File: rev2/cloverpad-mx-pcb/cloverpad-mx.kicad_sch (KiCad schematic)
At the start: 42 parts, among them J1 USB_C_Receptacle_USB2.0, SW1 SW_Push, SW2 SW_Push, U1 SRV05-4, U2 XC6206P332MR, U8 RP2040, U9 W25Q16JVSSIQ, Y1 12MHz

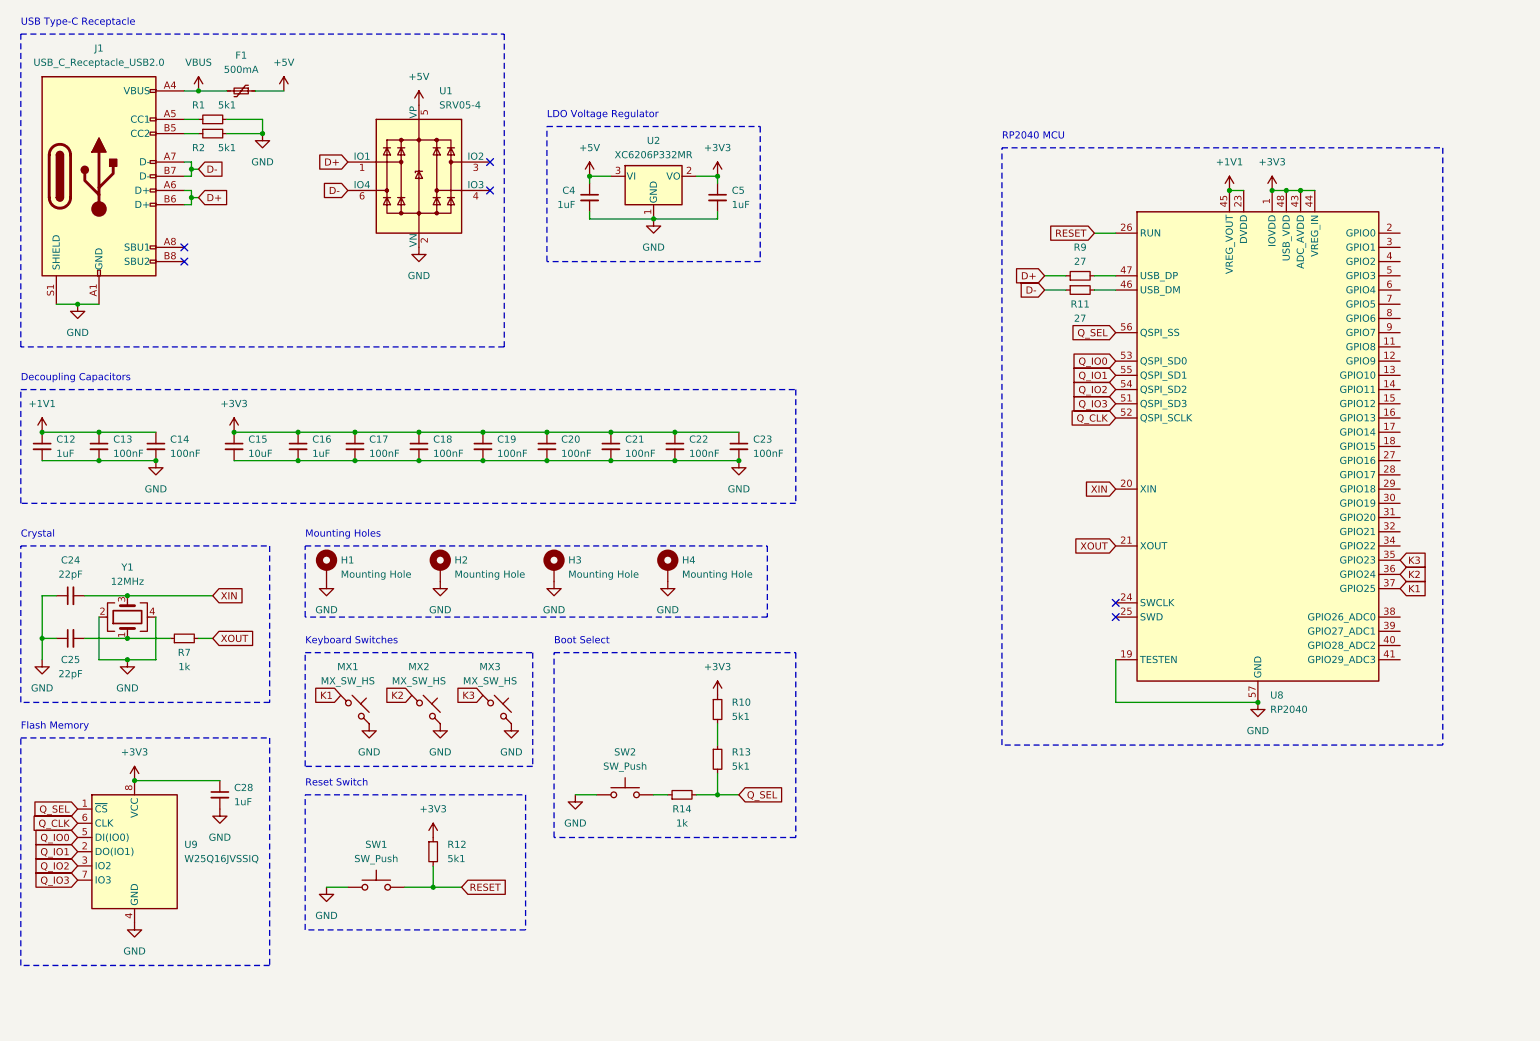
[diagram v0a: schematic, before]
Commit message: chore: update all symbols + footprints to match kicad 8
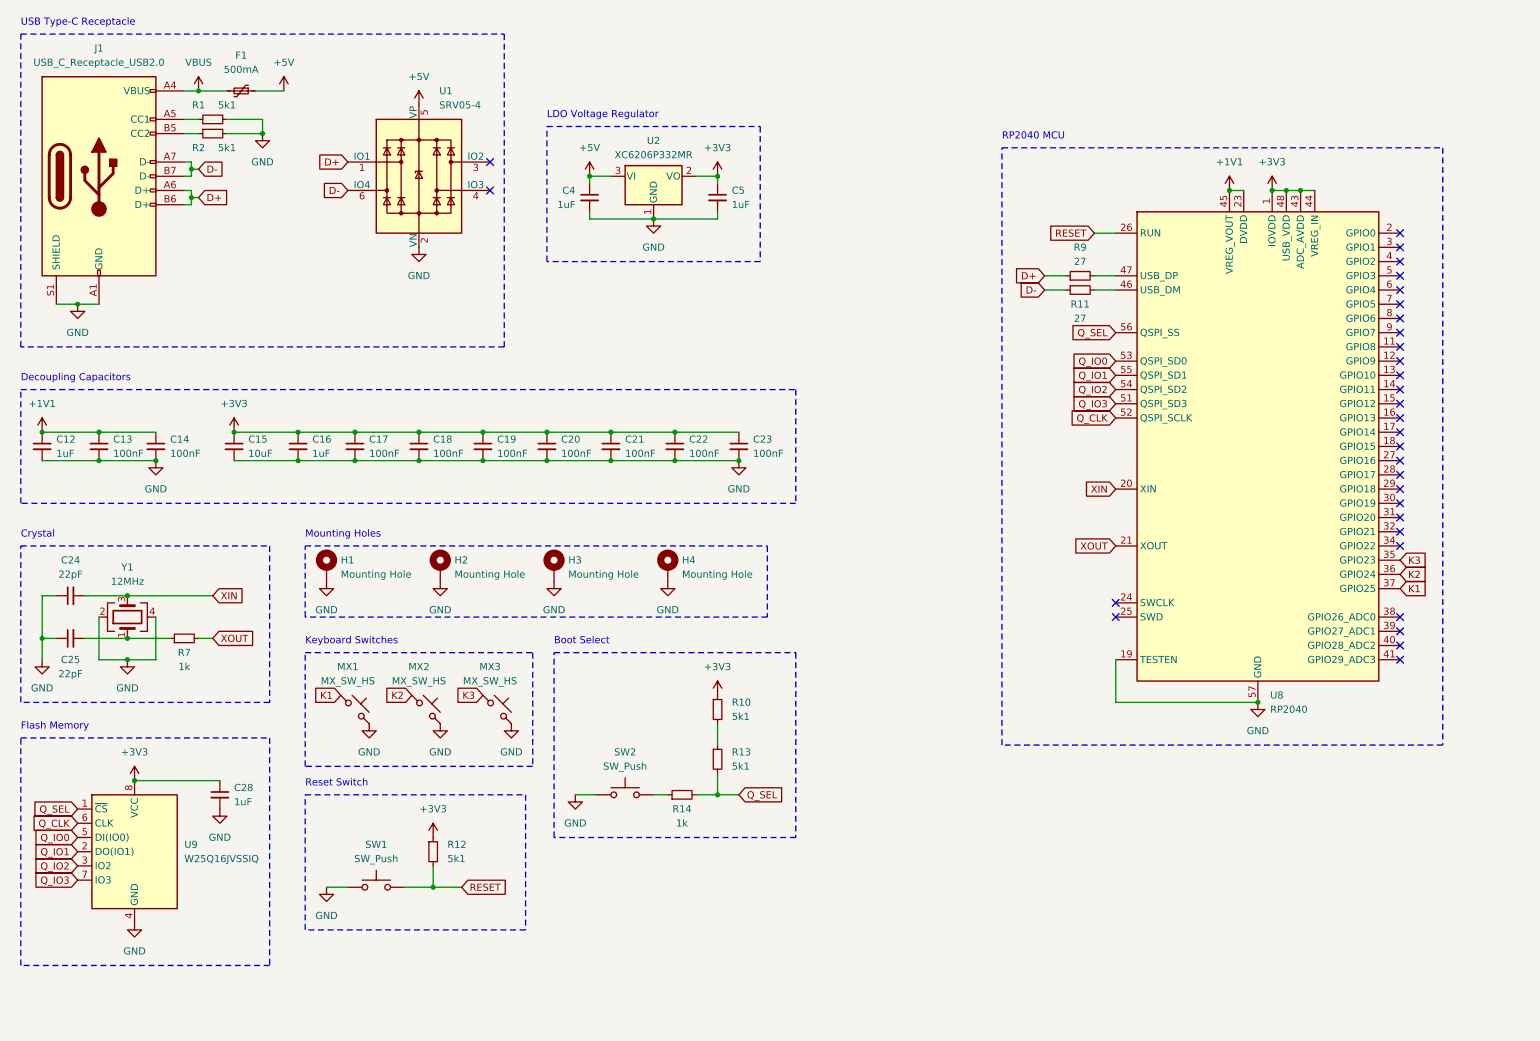
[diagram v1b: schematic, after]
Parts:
- J1: symbol Connector:USB_C_Receptacle_USB2.0 -> Connector:USB_C_Receptacle_USB2.0_14P
- MX1, MX2, MX3: footprint PCM_marbastlib-mx:SW_MX_HS_1u -> PCM_marbastlib-mx:SW_MX_HS_CPG151101S11_1u; symbol PCM_marbastlib-mx:MX_SW_HS -> PCM_marbastlib-mx:MX_SW_HS_CPG151101S11
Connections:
- no-connect marks 6 -> 31

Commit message: feat: new schematic for rev. 2, with various fixes and component changes
almost there - just need to figure out how to attach an EEPROM.
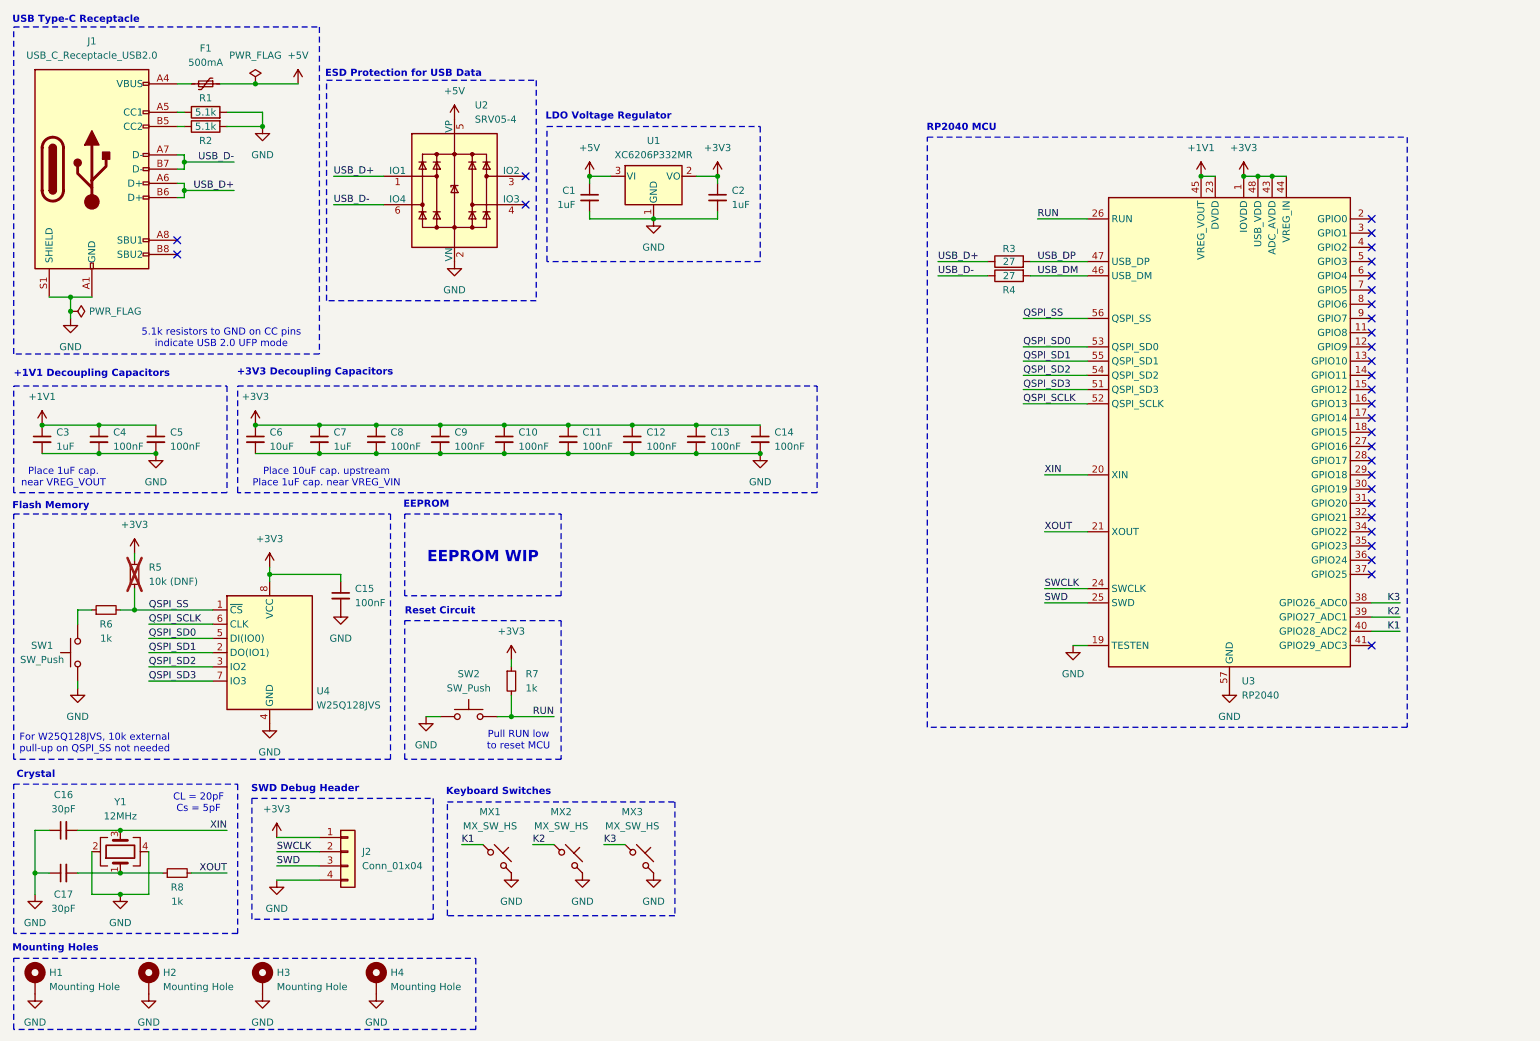
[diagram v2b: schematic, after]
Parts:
- removed R10: 5k1, Resistor_SMD:R_0402_1005Metric, symbol Device:R_Small
- added J2: Conn_01x04, Connector_PinHeader_2.54mm:PinHeader_1x04_P2.54mm_Horizontal, symbol Connector_Generic:Conn_01x04
- C15: renamed from C28; value 1uF -> 100nF; LCSC C52923 -> C1525
- C16: renamed from C24; value 22pF -> 30pF; footprint Capacitor_SMD:C_0402_1005Metric -> Capacitor_SMD:C_0603_1608Metric; LCSC C1555 -> C1658
- C17: renamed from C25; value 22pF -> 30pF; footprint Capacitor_SMD:C_0402_1005Metric -> Capacitor_SMD:C_0603_1608Metric; LCSC C1555 -> C1658
- J1: symbol Connector:USB_C_Receptacle_USB2.0_14P -> Connector:USB_C_Receptacle_USB2.0_16P
- R1, R2: value 5k1 -> 5.1k; symbol Device:R_Small -> Device:R
- R3: renamed from R9; symbol Device:R_Small -> Device:R; LCSC C25100 -> C140174
- R4: renamed from R11; symbol Device:R_Small -> Device:R; LCSC C25100 -> C140174
- R5: renamed from R13; value 5k1 -> 10k (DNF); LCSC C25905 -> (none); now not fitted; now left out of the parts list
- R7: renamed from R12; value 5k1 -> 1k; LCSC C25905 -> C11702
- U2: renamed from U1; LCSC C2836319 -> C20615829
- U4: renamed from U9; value W25Q16JVSSIQ -> W25Q128JVS; LCSC C131025 -> C97521
- renumbered C4 to C1, C19 to C10, C20 to C11, C21 to C12, C22 to C13, C23 to C14, C5 to C2, C12 to C3, C13 to C4, C14 to C5, C15 to C6, C16 to C7, C17 to C8, C18 to C9, R14 to R6, R7 to R8, SW2 to SW1, SW1 to SW2, U2 to U1, U8 to U3
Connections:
- net +3V3: now also R5.1, J2.1 (Pin_1)
- net GND: now also J2.4 (Pin_4)
- net K1: now also U3.40 (GPIO28_ADC2); no longer U3.37 (GPIO25)
- net K2: now also U3.39 (GPIO27_ADC1); no longer U3.36 (GPIO24)
- net K3: now also U3.38 (GPIO26_ADC0); no longer U3.35 (GPIO23)
- net USB_DP: now reaches R3.2, U3.47 (USB_DP)
- net USB_DM: now reaches R4.2, U3.46 (USB_DM)
- net SWCLK: now reaches U3.24 (SWCLK)
- net SWCLK: now also J2.2 (Pin_2)
- net SWD: now reaches U3.25 (SWD)
- net SWD: now also J2.3 (Pin_3)
- net D+ renamed USB_D+
- net D- renamed USB_D-
- net Q_CLK renamed QSPI_SCLK
- net Q_IO0 renamed QSPI_SD0
- net Q_IO1 renamed QSPI_SD1
- net Q_IO2 renamed QSPI_SD2
- net Q_IO3 renamed QSPI_SD3
- net Q_SEL renamed QSPI_SS
- net RESET renamed RUN
- net VBUS: no longer names the net of F1.2, J1.A4 (VBUS), J1.A9 (VBUS), J1.B4 (VBUS), J1.B9 (VBUS)
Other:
- note added: "+1V1 Decoupling Capacitors"
- note added: "+3V3 Decoupling Capacitors"
- note added: "5.1k resistors to GND on CC pins indicate USB 2.0 UFP mode"
- note added: "CL = 20pF Cs = 5pF"
- note added: "EEPROM"
- note added: "EEPROM WIP"
- note added: "ESD Protection for USB Data"
- note added: "For W25Q128JVS, 10k external pull-up on QSPI_SS not needed"
- note added: "Place 10uF cap. upstream Place 1uF cap. near VREG_VIN"
- note added: "Place 1uF cap. near VREG_VOUT"
- note added: "Pull RUN low to reset MCU"
- note added: "Reset Circuit"
- note added: "SWD Debug Header"
- note removed: "Boot Select"
- note removed: "Decoupling Capacitors"
- note removed: "Reset Switch"
- moved on the sheet: C10, C11, C12, C13, C14, C15, C16, C17, C3, C4, C5, C6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

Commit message: feat: add external AT24C32 EEPROM
for 3.3V, it seems that anything from 2k to 4.7k will work, but I've seen 10k working on Adafruit's EEPROM breakout. I've chosen 5.1k to minimise the BOM (the same ones used for USB).
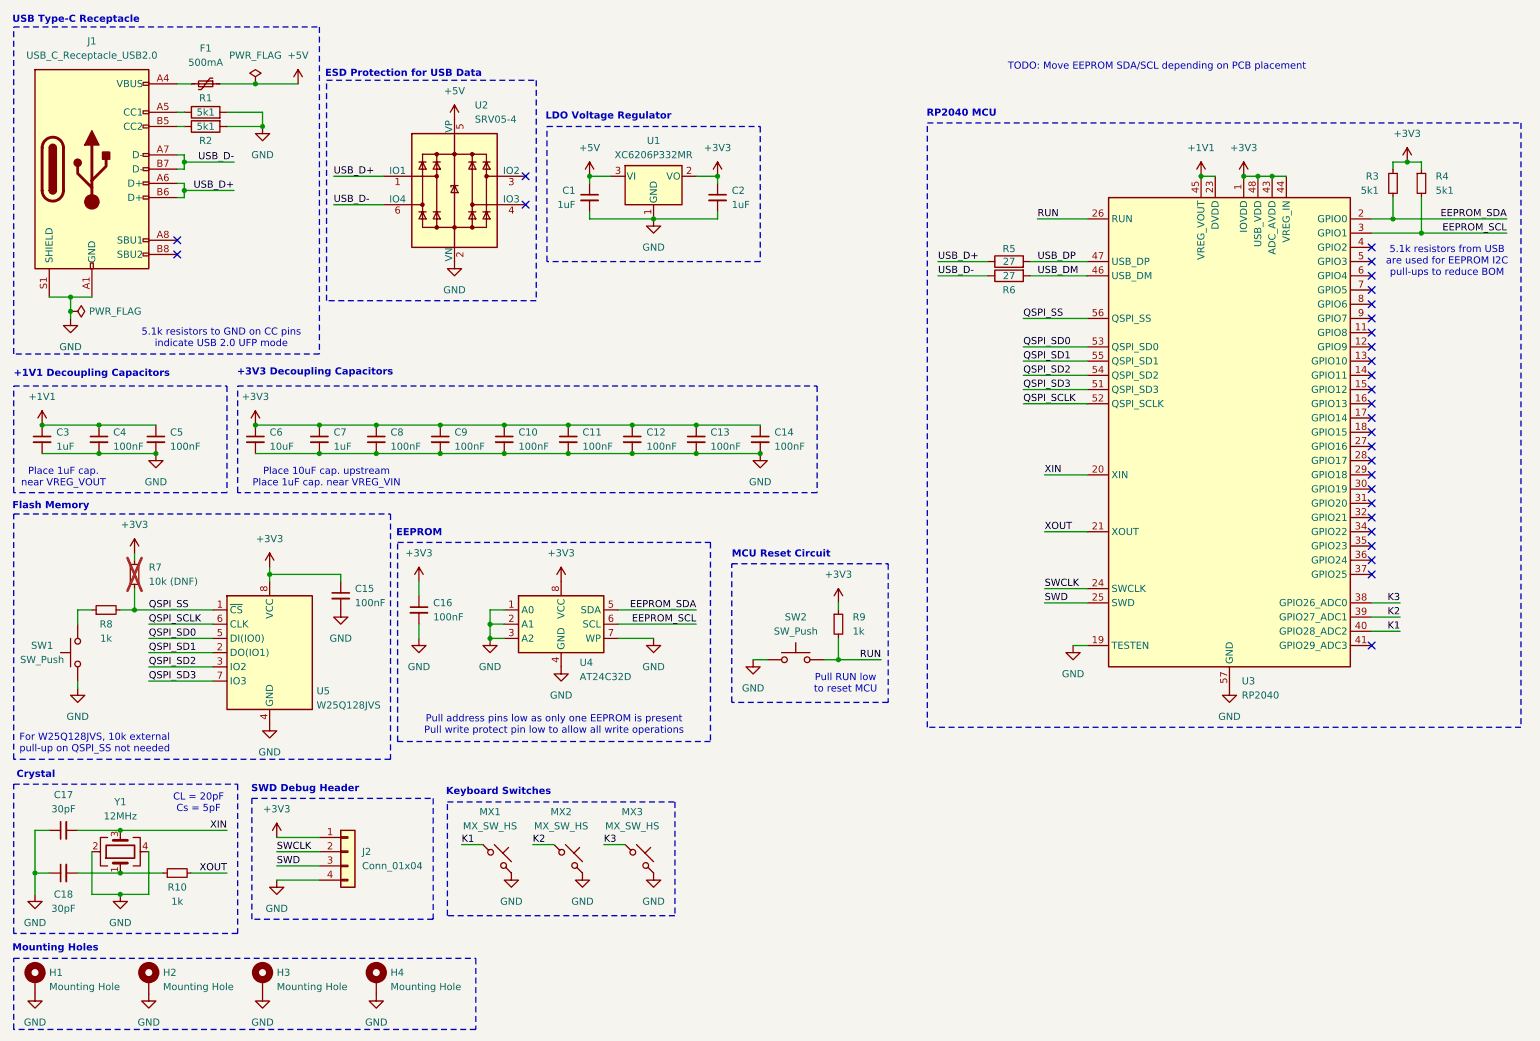
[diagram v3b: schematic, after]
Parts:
- added C16: 100nF, Capacitor_SMD:C_0402_1005Metric, symbol Device:C_Small
- added R3, R4: 5k1, Resistor_SMD:R_0402_1005Metric, symbol Device:R_Small
- added U4: AT24C32D, Package_SO:SOIC-8_3.9x4.9mm_P1.27mm, symbol Memory_EEPROM:24LC32
- R1, R2: value 5.1k -> 5k1
- renumbered C16 to C17, C17 to C18, R8 to R10, R3 to R5, R4 to R6, R5 to R7, R6 to R8, R7 to R9, U4 to U5
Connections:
- net +3V3: now also C16.1, R3.1, R4.1, U4.8 (VCC)
- net GND: now also C16.2, U4.1 (A0), U4.2 (A1), U4.3 (A2), U4.4 (GND), U4.7 (WP)
- net EEPROM_SDA: now reaches U3.2 (GPIO0)
- net EEPROM_SDA: now also R3.2, U4.5 (SDA)
- net EEPROM_SCL: now reaches U3.3 (GPIO1)
- net EEPROM_SCL: now also R4.2, U4.6 (SCL)
- no-connect marks 31 -> 29
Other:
- note added: "5.1k resistors from USB are used for EEPROM I2C pull-ups to reduce BOM"
- note added: "MCU Reset Circuit"
- note added: "Pull address pins low as only one EEPROM is present Pull write protect pin low to allow all write operations"
- note added: "TODO: Move EEPROM SDA/SCL depending on PCB placement"
- note removed: "EEPROM WIP"
- note removed: "Reset Circuit"
- moved on the sheet: R9, SW2
